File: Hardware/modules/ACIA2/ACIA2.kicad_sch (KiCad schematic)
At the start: 43 parts, among them J1 COM1/3, J2 COM2/4, J3 PORT1, J4 PORT2, J5 Bus_PCI_6502, U1 MAX232, U2 MAX232, U3 6551, U4 MAX232, U5 MAX232, U6 6551, U7 74HC138, U8 74HC138, X1 1.8432MHz

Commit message: Hardware Update Add MyCPU VGA Module Beautify all Schematics minor Error corrections Readme Update
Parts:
- JP4: value ACIA1/3 -> ACIA2/4
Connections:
- net A10: no longer names the net of J5.B9 (A10)
- net A11: no longer names the net of J5.A9 (A11)
- net A12: no longer names the net of J5.B11 (A12)
- net A13: no longer names the net of J5.A11 (A13)
- net A14: no longer names the net of J5.B12 (A14)
- net A15: no longer names the net of J5.A12 (A15)
- net A8: no longer names the net of J5.B8 (A8)
- net A9: no longer names the net of J5.A8 (A9)
- net E: no longer names the net of J5.A45 (E)
- net M/X: no longer names the net of J5.B46 (M/~{X})
- net PAGE: no longer names the net of J5.B34 (PAGE_ROM)
- net RAM_0: no longer names the net of J5.A53 (RAM0)
- net RAM_1: no longer names the net of J5.A54 (RAM1)
- net RAM_2: no longer names the net of J5.A55 (RAM2)
- net RAM_3: no longer names the net of J5.A56 (RAM3)
- net RAM_4: no longer names the net of J5.A58 (RAM4)
- net RAM_5: no longer names the net of J5.A59 (RAM5)
- net RAM_6: no longer names the net of J5.A60 (RAM6)
- net RAM_7: no longer names the net of J5.A61 (RAM7)
- net ROM_0: no longer names the net of J5.B53 (ROM0)
- net ROM_1: no longer names the net of J5.B54 (ROM1)
- net ROM_2: no longer names the net of J5.B55 (ROM2)
- net ROM_3: no longer names the net of J5.B56 (ROM3)
- net ROM_4: no longer names the net of J5.B58 (ROM4)
- net ROM_5: no longer names the net of J5.B59 (ROM5)
- net ROM_6: no longer names the net of J5.B60 (ROM6)
- net ROM_7: no longer names the net of J5.B61 (ROM7)
- net SYNC_VPA: no longer names the net of J5.A38 (Sync/VPA)
- net ~{BE}: no longer names the net of J5.A42 (~{BE})
- net ~{H_RAM}: no longer names the net of J5.B25 (~{H_RAM})
- net ~{IRQ_0.4}: no longer names the net of J5.A31 (~{IRQ_0.4})
- net ~{IRQ_0.5}: no longer names the net of J5.A32 (~{IRQ_0.5})
- net ~{IRQ_0.6}: no longer names the net of J5.A33 (~{IRQ_0.6})
- net ~{IRQ_0.7}: no longer names the net of J5.A34 (~{IRQ_0.7})
- net ~{IRQ_0}: no longer names the net of J5.B28 (~{IRQ_0})
- net ~{IRQ_1}: no longer names the net of J5.B29 (~{IRQ_1})
- net ~{IRQ_2}: no longer names the net of J5.B30 (~{IRQ_2})
- net ~{IRQ_3}: no longer names the net of J5.B31 (~{IRQ_3})
- net ~{IRQ_4}: no longer names the net of J5.B32 (~{IRQ_4})
- net ~{IRQ}: no longer names the net of J5.B27 (~{IRQ})
- net ~{L_RAM}: no longer names the net of J5.B24 (~{L_RAM})
- net ~{ML}: no longer names the net of J5.B39 (~{ML})
- net ~{NMI}: no longer names the net of J5.B33 (~{NMI})
- net ~{RDY}: no longer names the net of J5.A41 (~{RDY})
- net ~{ROM}: no longer names the net of J5.A25 (~{ROM})
- net ~{VP}: no longer names the net of J5.B38 (~{VP})
- net Ø2/VDA: no longer names the net of J5.A39 (Ø2/VDA)
- no-connect marks 21 -> 68
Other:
- note added: "ACIA 1"
- note added: "ACIA 2"
- note added: "Bus Connector"
- note added: "Decoupling"
- note added: "Dual ACIA UART Interface"
- company: (none) -> Synthron
- title: (none) -> S65xx Computer System
- moved on the sheet: C10, C11, C12, C13, C14, C15, C16, C17, C18, C19, C20, C21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

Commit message: finalize overview schematic
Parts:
- renumbered C1 to C26, C2 to C27, C3 to C28, C4 to C29, C5 to C30, C6 to C31, C7 to C32, C8 to C33, C9 to C34, C10 to C35, C11 to C36, C12 to C37, C13 to C38, C14 to C39, C15 to C40, C16 to C41, C17 to C42, C18 to C43, C19 to C44, C20 to C45, C21 to C46, C22 to C47, C23 to C48, C24 to C49, C25 to C50, J2 to J10, J4 to J11, J5 to J12, J1 to J8, J3 to J9, JP1 to JP17, JP2 to JP18, JP3 to JP19, JP4 to JP20, U2 to U10, U3 to U11, U4 to U12, U5 to U13, U6 to U14, U7 to U15, U8 to U16, U1 to U9, X1 to X2

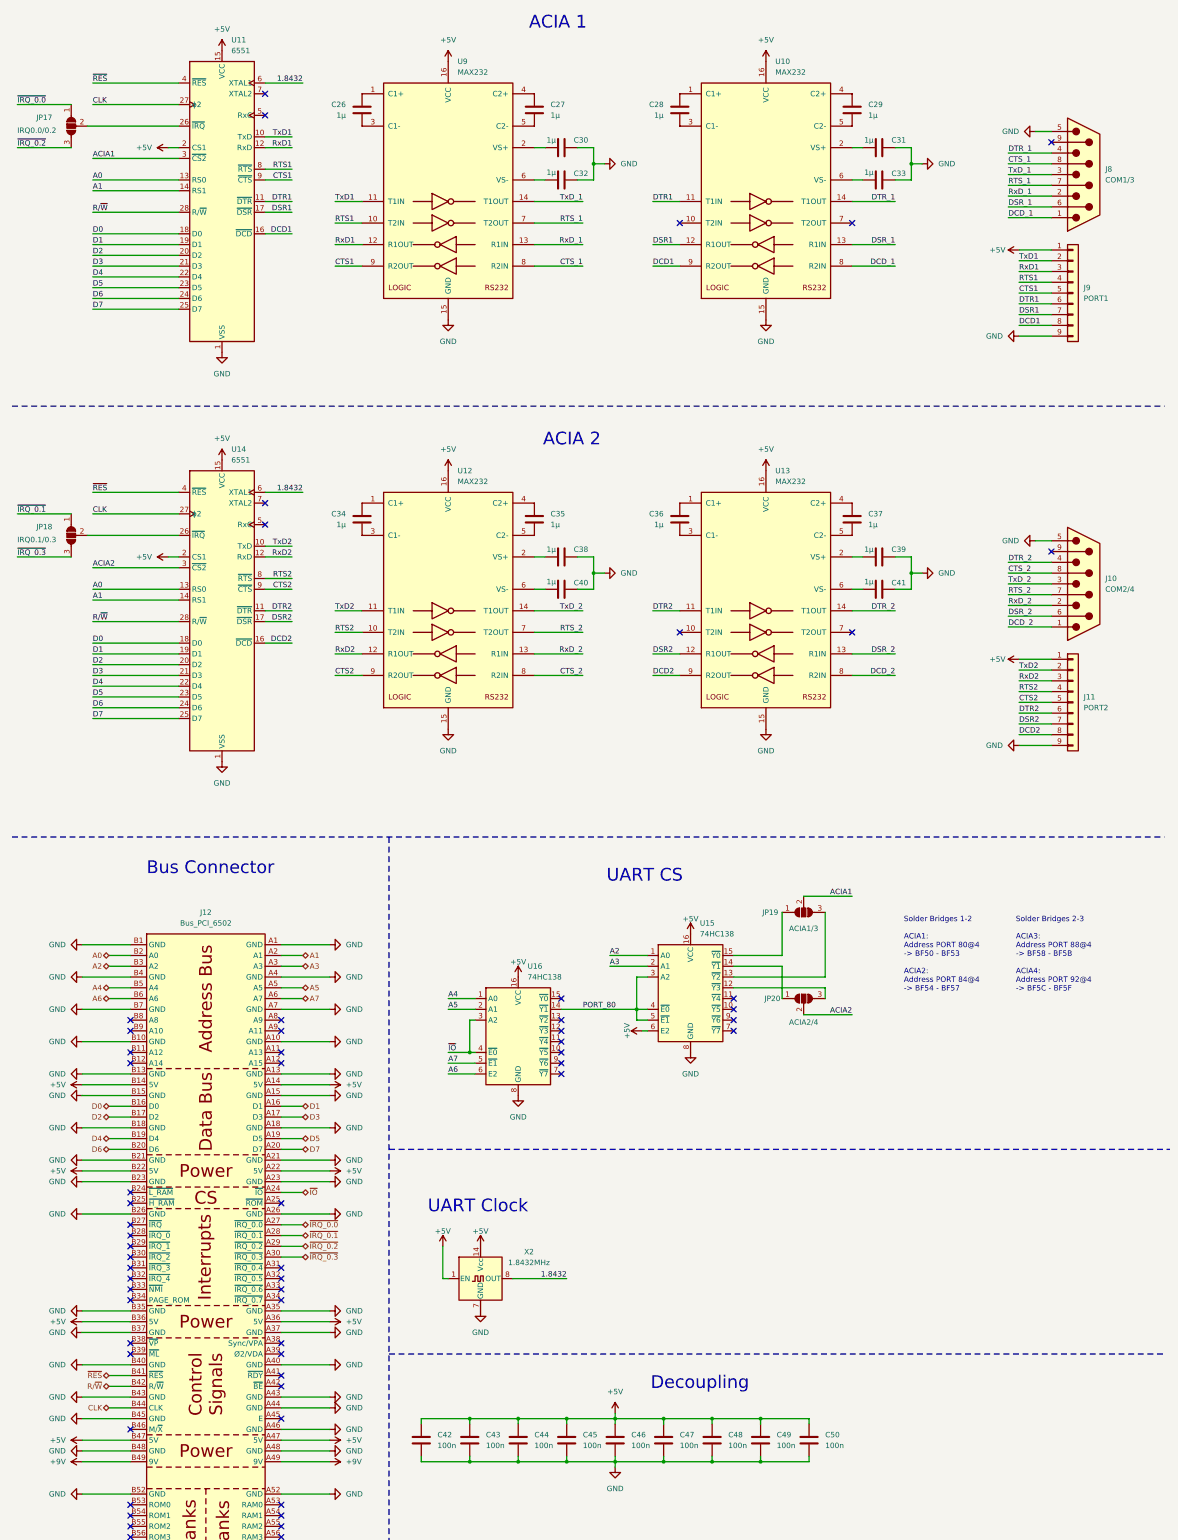
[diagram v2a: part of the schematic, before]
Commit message: Hardware Review Pt. 1 fix Address Decoding for Strobe Generators add bulk capacitance to every board fix wiring of Prototyping Board
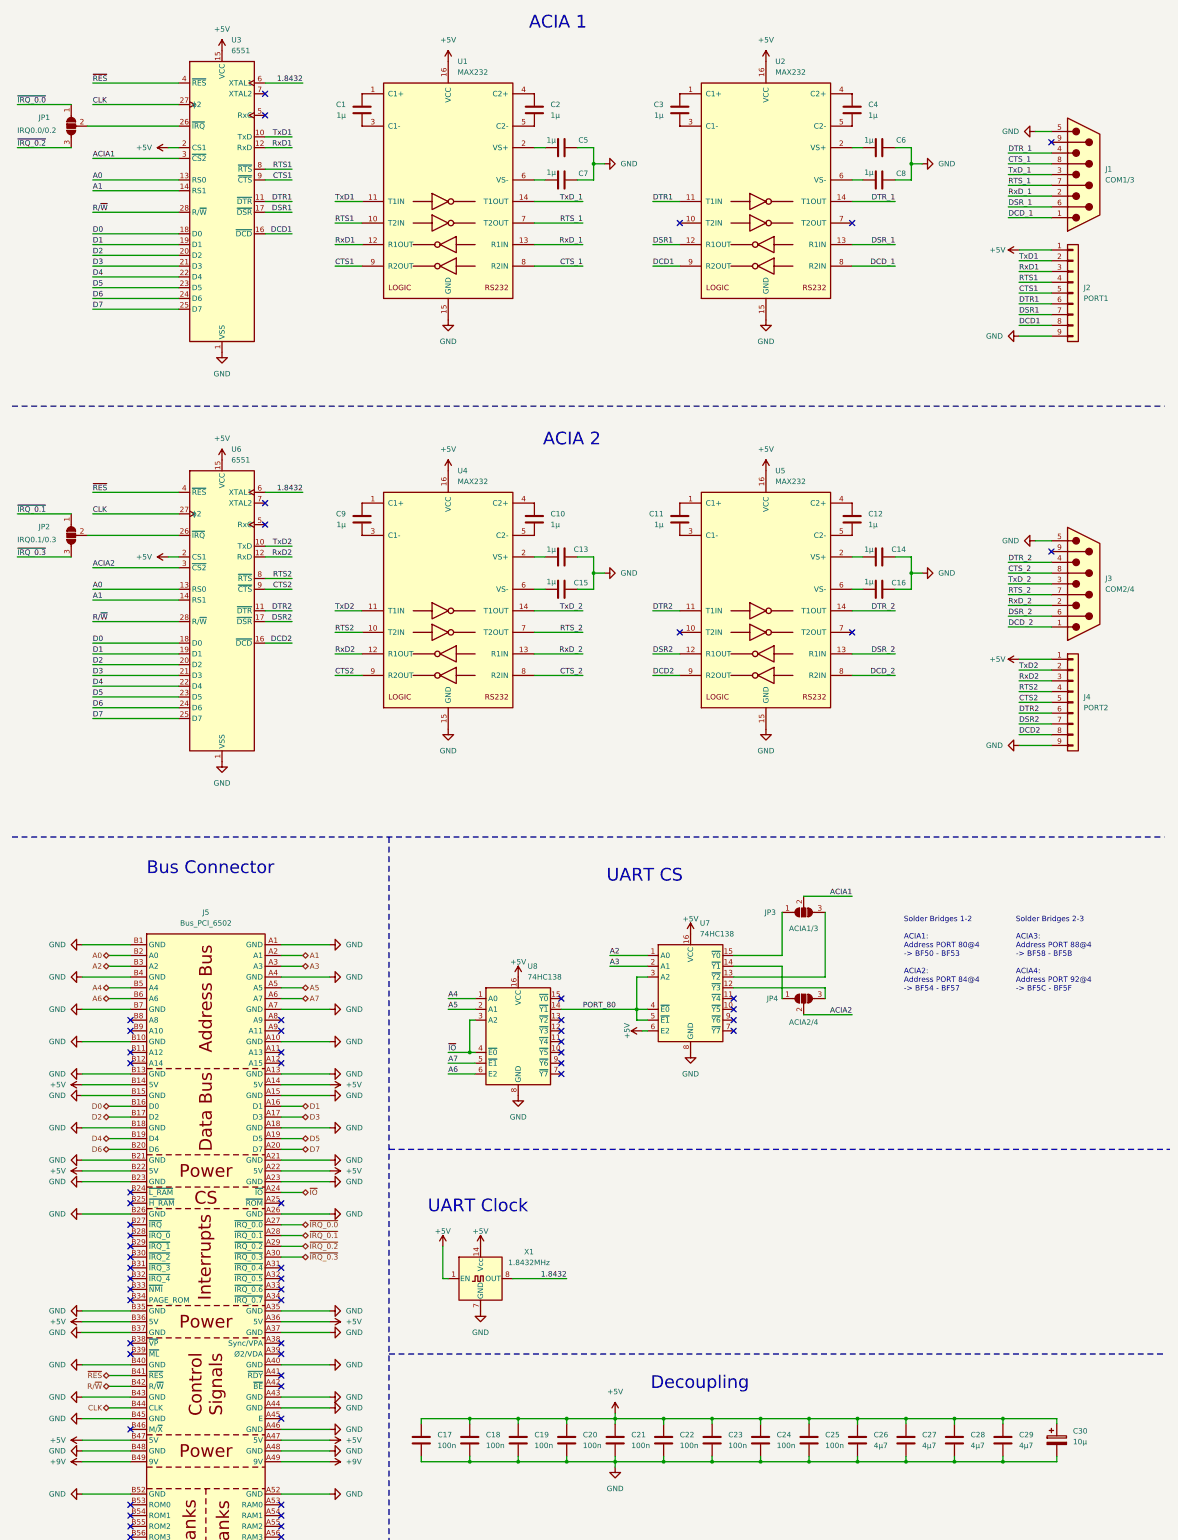
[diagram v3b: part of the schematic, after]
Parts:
- added C26, C27, C28, C29: 4µ7, Capacitor_SMD:C_0805_2012Metric, symbol Device:C
- added C30: 10µ, Capacitor_THT:CP_Radial_D5.0mm_P2.50mm, symbol Device:C_Polarized
- renumbered C26 to C1, C35 to C10, C36 to C11, C37 to C12, C38 to C13, C39 to C14, C40 to C15, C41 to C16, C42 to C17, C43 to C18, C44 to C19, C27 to C2, C45 to C20, C46 to C21, C47 to C22, C48 to C23, C49 to C24, C50 to C25, C28 to C3, C29 to C4, C30 to C5, C31 to C6, C32 to C7, C33 to C8, C34 to C9, J8 to J1, J9 to J2, J10 to J3, J11 to J4, J12 to J5, JP17 to JP1, JP18 to JP2, JP19 to JP3, JP20 to JP4, U9 to U1, U10 to U2, U11 to U3, U12 to U4, U13 to U5, U14 to U6, U15 to U7, U16 to U8, X2 to X1
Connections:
- net +5V: now also C26.1, C27.1, C28.1, C29.1, C30.1
- net GND: now also C26.2, C27.2, C28.2, C29.2, C30.2
